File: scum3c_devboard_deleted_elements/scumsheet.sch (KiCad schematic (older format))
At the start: 16 parts, among them P5 Conn_01x02, U8 scum3

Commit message: added placeholder battery
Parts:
- removed P5: Conn_01x02, Connector_PinHeader_2.54mm:PinHeader_1x02_P2.54mm_Vertical, symbol Connector_Generic:Conn_01x02
- added BT1: Battery_Cell, symbol Device:Battery_Cell
- added P5: Conn_01x03, Connector_PinHeader_2.54mm:PinHeader_1x03_P2.54mm_Vertical, symbol Connector_Generic:Conn_01x03
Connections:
- wire segments 26 -> 23
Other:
- note added: "i know this isn't how it works. just getting a footprint placeholder\n"
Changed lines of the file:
@@
 GPIO0
-$Comp
-L Connector_Generic:Conn_01x02 P5
-U 1 1 5F3A4822
-P 9700 4850
-F 0 "P5" H 9618 5067 50  0000 C CNN
-F 1 "Conn_01x02" H 9618 4976 50  0000 C CNN
-F 2 "Connector_PinHeader_2.54mm:PinHeader_1x02_P2.54mm_Vertical" H 9700 4850 50  0001 C CNN
-F 3 "~" H 9700 4850 50  0001 C CNN
-	1    9700 4850
-	-1   0    0    -1
-$EndComp
 $Comp
 L draft1library:+VBAT #PWR0210
 U 1 1 5F3AF896
-P 10150 5050
+P 9800 5650
 AR Path="/5F3B1D81/5F3AF896" Ref="#PWR0210"  Part="1"
 AR Path="/5F41418C/5F3AF896" Ref="#PWR?"  Part="1"
 AR Path="/5F414989/5F3AF896" Ref="#PWR?"  Part="1"
-F 0 "#PWR0210" H 10150 4900 50  0001 C CNN
-F 1 "+VBAT" H 10165 5223 50  0000 C CNN
-F 2 "" H 10150 5050 50  0001 C CNN
-F 3 "" H 10150 5050 50  0001 C CNN
-	1    10150 5050
-	-1   0    0    1
+F 0 "#PWR0210" H 9800 5500 50  0001 C CNN
+F 1 "+VBAT" V 9800 5900 50  0000 C CNN
+F 2 "" H 9800 5650 50  0001 C CNN
+F 3 "" H 9800 5650 50  0001 C CNN
+	1    9800 5650
+	0    1    1    0
 $EndComp
-Wire Wire Line
-	10150 4950 10150 5050
-Wire Wire Line
-	9900 4950 10150 4950
-Wire Wire Line
-	9900 4850 10800 4850
-Text Label 10800 4850 2    50   ~ 0
+Text Label 9800 5450 0    50   ~ 0
 BOOT_SOURCE_SEL
 Wire Wire Line
@@
 	4750 6500 4750 6050
 $Comp
-L power:GND #PWR?
+L power:GND #PWR0109
 U 1 1 5F4F714B
 P 2250 4100
-AR Path="/5F3B1D81/5F4F714B" Ref="#PWR?"  Part="1"
+AR Path="/5F3B1D81/5F4F714B" Ref="#PWR0109"  Part="1"
 AR Path="/5F41418C/5F4F714B" Ref="#PWR?"  Part="1"
 AR Path="/5F414989/5F4F714B" Ref="#PWR?"  Part="1"
-F 0 "#PWR?" H 2250 3850 50  0001 C CNN
+F 0 "#PWR0109" H 2250 3850 50  0001 C CNN
 F 1 "GND" V 2255 3972 50  0000 R CNN
 F 2 "" H 2250 4100 50  0001 C CNN
@@
 NoConn ~ 6900 6050
 NoConn ~ 7050 6050
+$Comp
+L Connector_Generic:Conn_01x03 P5
+U 1 1 5F5126D4
+P 9600 5550
+F 0 "P5" H 9518 5225 50  0000 C CNN
+F 1 "Conn_01x03" H 9518 5316 50  0000 C CNN
+F 2 "Connector_PinHeader_2.54mm:PinHeader_1x03_P2.54mm_Vertical" H 9600 5550 50  0001 C CNN
+F 3 "~" H 9600 5550 50  0001 C CNN
+	1    9600 5550
+	-1   0    0    1
+$EndComp
+$Comp
+L draft1library:+VDDIO #PWR0110
+U 1 1 5F5148F6
+P 9800 5550
+F 0 "#PWR0110" H 9800 5400 50  0001 C CNN
+F 1 "+VDDIO" V 9815 5678 50  0000 L CNN
+F 2 "" H 9800 5550 50  0001 C CNN
+F 3 "" H 9800 5550 50  0001 C CNN
+	1    9800 5550
+	0    1    1    0
+$EndComp
+$Comp
+L Device:Battery_Cell BT1
+U 1 1 5F554877
+P 10300 4300
+F 0 "BT1" H 10418 4396 50  0000 L CNN
+F 1 "Battery_Cell" H 10418 4305 50  0000 L CNN
+F 2 "" V 10300 4360 50  0001 C CNN
+F 3 "~" V 10300 4360 50  0001 C CNN
+	1    10300 4300
+	1    0    0    -1
+$EndComp
+$Comp
+L power:GND #PWR0120
+U 1 1 5F555029
+P 10300 4400
+F 0 "#PWR0120" H 10300 4150 50  0001 C CNN
+F 1 "GND" H 10305 4227 50  0000 C CNN
+F 2 "" H 10300 4400 50  0001 C CNN
+F 3 "" H 10300 4400 50  0001 C CNN
+	1    10300 4400
+	1    0    0    -1
+$EndComp
+$Comp
+L draft1library:+VBAT #PWR0121
+U 1 1 5F5558C9
+P 10300 4100
+F 0 "#PWR0121" H 10300 3950 50  0001 C CNN
+F 1 "+VBAT" H 10315 4273 50  0000 C CNN
+F 2 "" H 10300 4100 50  0001 C CNN
+F 3 "" H 10300 4100 50  0001 C CNN
+	1    10300 4100
+	1    0    0    -1
+$EndComp
+Text Notes 8600 4850 0    50   ~ 0
+i know this isn't how it works. just getting a footprint placeholder\n
 $EndSCHEMATC

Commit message: battery footprint
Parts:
- BT1: footprint (none) -> Battery:Battery_Panasonic_CR2032-VS1N_Vertical_CircularHoles
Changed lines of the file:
@@
-$EndComp
-$Comp
-L Device:Battery_Cell BT1
-U 1 1 5F554877
-P 10300 4300
-F 0 "BT1" H 10418 4396 50  0000 L CNN
-F 1 "Battery_Cell" H 10418 4305 50  0000 L CNN
-F 2 "" V 10300 4360 50  0001 C CNN
-F 3 "~" V 10300 4360 50  0001 C CNN
-	1    10300 4300
-	1    0    0    -1
 $EndComp
 $Comp
@@
 Text Notes 8600 4850 0    50   ~ 0
 i know this isn't how it works. just getting a footprint placeholder\n
+$Comp
+L Device:Battery_Cell BT1
+U 1 1 5F554877
+P 10300 4300
+F 0 "BT1" H 10418 4396 50  0000 L CNN
+F 1 "Battery_Cell" H 10418 4305 50  0000 L CNN
+F 2 "Battery:Battery_Panasonic_CR2032-VS1N_Vertical_CircularHoles" V 10300 4360 50  0001 C CNN
+F 3 "~" V 10300 4360 50  0001 C CNN
+	1    10300 4300
+	1    0    0    -1
+$EndComp
 $EndSCHEMATC

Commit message: added zener diode voltage protection
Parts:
- U8: footprint SCUM:QFN-100_EP_12x12_Pitch0.4mm -> SCUM:QFN-100_EP_12x12_Pitch0.4mm_Margin0.25mm
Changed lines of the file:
@@
 Wire Wire Line
 	4750 6500 4750 6050
-$Comp
-L power:GND #PWR0109
-U 1 1 5F4F714B
-P 2250 4100
-AR Path="/5F3B1D81/5F4F714B" Ref="#PWR0109"  Part="1"
-AR Path="/5F41418C/5F4F714B" Ref="#PWR?"  Part="1"
-AR Path="/5F414989/5F4F714B" Ref="#PWR?"  Part="1"
-F 0 "#PWR0109" H 2250 3850 50  0001 C CNN
-F 1 "GND" V 2255 3972 50  0000 R CNN
-F 2 "" H 2250 4100 50  0001 C CNN
-F 3 "" H 2250 4100 50  0001 C CNN
-	1    2250 4100
-	0    1    1    0
-$EndComp
 NoConn ~ 8000 3000
 NoConn ~ 8000 3150
@@
 F 0 "U8" H 8944 3271 50  0000 L CNN
 F 1 "scum3" H 8944 3180 50  0000 L CNN
-F 2 "SCUM:QFN-100_EP_12x12_Pitch0.4mm" H 5200 3450 50  0001 C CNN
+F 2 "SCUM:QFN-100_EP_12x12_Pitch0.4mm_Margin0.25mm" H 5200 3450 50  0001 C CNN
 F 3 "" H 5200 3450 50  0001 C CNN
 	1    5200 3450
@@
 	1    0    0    -1
 $EndComp
+$Comp
+L power:GND #PWR0109
+U 1 1 5F4F714B
+P 2250 4100
+AR Path="/5F3B1D81/5F4F714B" Ref="#PWR0109"  Part="1"
+AR Path="/5F41418C/5F4F714B" Ref="#PWR?"  Part="1"
+AR Path="/5F414989/5F4F714B" Ref="#PWR?"  Part="1"
+F 0 "#PWR0109" H 2250 3850 50  0001 C CNN
+F 1 "GND" V 2255 3972 50  0000 R CNN
+F 2 "" H 2250 4100 50  0001 C CNN
+F 3 "" H 2250 4100 50  0001 C CNN
+	1    2250 4100
+	0    1    1    0
+$EndComp
 $EndSCHEMATC

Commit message: added LED
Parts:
- removed BT1: Battery_Cell, Battery:Battery_Panasonic_CR2032-VS1N_Vertical_CircularHoles, symbol Device:Battery_Cell
- removed P5: Conn_01x03, Connector_PinHeader_2.54mm:PinHeader_1x03_P2.54mm_Vertical, symbol Connector_Generic:Conn_01x03
- added LED1: LD_MVSG-JGLH-46-1, LEDM2218X140N, symbol SamacSys_Parts:LD_MVSG-JGLH-46-1
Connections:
- net labels added: 3WB_CLK, 3WB_DATA, 3WB_ENB, RF_IN, RsRx, RsTx
- wire segments 23 -> 24
- no-connect marks 58 -> 52
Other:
- note removed: "i know this isn't how it works. just getting a footprint placeholder\n"
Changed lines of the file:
@@
 NoConn ~ 8000 2100
 NoConn ~ 8000 2250
-NoConn ~ 8000 4650
 NoConn ~ 8000 5550
 NoConn ~ 8000 5400
@@
 Wire Wire Line
 	8000 4050 9250 4050
-Text Label 9250 4050 2    50   ~ 0
-BOOT_SOURCE_SEL
 $Comp
 L Device:C C20
@@
 Text HLabel 3700 6050 3    50   BiDi ~ 0
 GPIO0
-$Comp
-L draft1library:+VBAT #PWR0210
-U 1 1 5F3AF896
-P 9800 5650
-AR Path="/5F3B1D81/5F3AF896" Ref="#PWR0210"  Part="1"
-AR Path="/5F41418C/5F3AF896" Ref="#PWR?"  Part="1"
-AR Path="/5F414989/5F3AF896" Ref="#PWR?"  Part="1"
-F 0 "#PWR0210" H 9800 5500 50  0001 C CNN
-F 1 "+VBAT" V 9800 5900 50  0000 C CNN
-F 2 "" H 9800 5650 50  0001 C CNN
-F 3 "" H 9800 5650 50  0001 C CNN
-	1    9800 5650
-	0    1    1    0
-$EndComp
-Text Label 9800 5450 0    50   ~ 0
-BOOT_SOURCE_SEL
 Wire Wire Line
 	4300 6050 4300 6500
@@
 	1    0    0    -1
 $EndComp
-NoConn ~ 6450 6050
-NoConn ~ 6600 6050
-NoConn ~ 6750 6050
-NoConn ~ 6900 6050
-NoConn ~ 7050 6050
-$Comp
-L Connector_Generic:Conn_01x03 P5
-U 1 1 5F5126D4
-P 9600 5550
-F 0 "P5" H 9518 5225 50  0000 C CNN
-F 1 "Conn_01x03" H 9518 5316 50  0000 C CNN
-F 2 "Connector_PinHeader_2.54mm:PinHeader_1x03_P2.54mm_Vertical" H 9600 5550 50  0001 C CNN
-F 3 "~" H 9600 5550 50  0001 C CNN
-	1    9600 5550
+Text HLabel 6750 6050 3    50   BiDi ~ 0
+3WB_CLK
+Text HLabel 6900 6050 3    50   BiDi ~ 0
+3WB_ENB
+Text HLabel 7050 6050 3    50   BiDi ~ 0
+3WB_DATA
+Text HLabel 2250 4100 0    50   BiDi ~ 0
+RF_IN
+Text HLabel 6450 6050 3    50   BiDi ~ 0
+RsTx
+Text HLabel 6600 6050 3    50   BiDi ~ 0
+RsRx
+Text HLabel 9250 4050 2    50   BiDi ~ 0
+BOOT_SOURCE_SEL
+$Comp
+L SamacSys_Parts:LD_MVSG-JGLH-46-1 LED1
+U 1 1 5F7B4972
+P 9200 4650
+F 0 "LED1" H 9500 4385 50  0000 C CNN
+F 1 "LD_MVSG-JGLH-46-1" H 9500 4476 50  0000 C CNN
+F 2 "LEDM2218X140N" H 9700 4800 50  0001 L BNN
+F 3 "https://dammedia.osram.info/media/resource/hires/osram-dam-6917470/LD%20MVSG_EN.pdf" H 9700 4700 50  0001 L BNN
+F 4 "Osram Opto LD MVSG-JGLH-46-1, Mini TOPLED Series Blue LED, 465 nm,, Rectangle Lens SMD Package" H 9700 4600 50  0001 L BNN "Description"
+F 5 "1.4" H 9700 4500 50  0001 L BNN "Height"
+F 6 "OSRAM" H 9700 4400 50  0001 L BNN "Manufacturer_Name"
+F 7 "LD MVSG-JGLH-46-1" H 9700 4300 50  0001 L BNN "Manufacturer_Part_Number"
+F 8 "LD MVSG-JGLH-46-1" H 9700 4200 50  0001 L BNN "Arrow Part Number"
+F 9 "https://www.arrow.com/en/products/ldmvsg-jglh-46-1/osram-opto-semiconductors" H 9700 4100 50  0001 L BNN "Arrow Price/Stock"
+F 10 "720-LDMVSGJGLH461" H 9700 4000 50  0001 L BNN "Mouser Part Number"
+F 11 "https://www.mouser.co.uk/ProductDetail/OSRAM-Opto-Semiconductors/LD-MVSG-JGLH-46-1?qs=znB0%2F8lYn%252BuYpqaPHtqGHw%3D%3D" H 9700 3900 50  0001 L BNN "Mouser Price/Stock"
+	1    9200 4650
 	-1   0    0    1
 $EndComp
-$Comp
-L draft1library:+VDDIO #PWR0110
-U 1 1 5F5148F6
-P 9800 5550
-F 0 "#PWR0110" H 9800 5400 50  0001 C CNN
-F 1 "+VDDIO" V 9815 5678 50  0000 L CNN
-F 2 "" H 9800 5550 50  0001 C CNN
-F 3 "" H 9800 5550 50  0001 C CNN
-	1    9800 5550
-	0    1    1    0
-$EndComp
-$Comp
-L power:GND #PWR0120
-U 1 1 5F555029
-P 10300 4400
-F 0 "#PWR0120" H 10300 4150 50  0001 C CNN
-F 1 "GND" H 10305 4227 50  0000 C CNN
-F 2 "" H 10300 4400 50  0001 C CNN
-F 3 "" H 10300 4400 50  0001 C CNN
-	1    10300 4400
-	1    0    0    -1
-$EndComp
-$Comp
-L draft1library:+VBAT #PWR0121
-U 1 1 5F5558C9
-P 10300 4100
-F 0 "#PWR0121" H 10300 3950 50  0001 C CNN
-F 1 "+VBAT" H 10315 4273 50  0000 C CNN
-F 2 "" H 10300 4100 50  0001 C CNN
-F 3 "" H 10300 4100 50  0001 C CNN
-	1    10300 4100
-	1    0    0    -1
-$EndComp
-Text Notes 8600 4850 0    50   ~ 0
-i know this isn't how it works. just getting a footprint placeholder\n
-$Comp
-L Device:Battery_Cell BT1
-U 1 1 5F554877
-P 10300 4300
-F 0 "BT1" H 10418 4396 50  0000 L CNN
-F 1 "Battery_Cell" H 10418 4305 50  0000 L CNN
-F 2 "Battery:Battery_Panasonic_CR2032-VS1N_Vertical_CircularHoles" V 10300 4360 50  0001 C CNN
-F 3 "~" V 10300 4360 50  0001 C CNN
-	1    10300 4300
-	1    0    0    -1
-$EndComp
-$Comp
-L power:GND #PWR0109
-U 1 1 5F4F714B
-P 2250 4100
-AR Path="/5F3B1D81/5F4F714B" Ref="#PWR0109"  Part="1"
-AR Path="/5F41418C/5F4F714B" Ref="#PWR?"  Part="1"
-AR Path="/5F414989/5F4F714B" Ref="#PWR?"  Part="1"
-F 0 "#PWR0109" H 2250 3850 50  0001 C CNN
-F 1 "GND" V 2255 3972 50  0000 R CNN
-F 2 "" H 2250 4100 50  0001 C CNN
-F 3 "" H 2250 4100 50  0001 C CNN
-	1    2250 4100
-	0    1    1    0
+Wire Wire Line
+	8000 4650 8600 4650
+$Comp
+L power:GND #PWR?
+U 1 1 5F7B7D3D
+P 9200 4650
+F 0 "#PWR?" H 9200 4400 50  0001 C CNN
+F 1 "GND" V 9205 4522 50  0000 R CNN
+F 2 "" H 9200 4650 50  0001 C CNN
+F 3 "" H 9200 4650 50  0001 C CNN
+	1    9200 4650
+	0    -1   -1   0
 $EndComp
 $EndSCHEMATC

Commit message: moved pins
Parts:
- LED1: footprint LEDM2218X140N -> SamacSys_Parts:LEDM2218X140N
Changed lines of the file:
@@
 F 0 "LED1" H 9500 4385 50  0000 C CNN
 F 1 "LD_MVSG-JGLH-46-1" H 9500 4476 50  0000 C CNN
-F 2 "LEDM2218X140N" H 9700 4800 50  0001 L BNN
+F 2 "SamacSys_Parts:LEDM2218X140N" H 9700 4800 50  0001 L BNN
 F 3 "https://dammedia.osram.info/media/resource/hires/osram-dam-6917470/LD%20MVSG_EN.pdf" H 9700 4700 50  0001 L BNN
 F 4 "Osram Opto LD MVSG-JGLH-46-1, Mini TOPLED Series Blue LED, 465 nm,, Rectangle Lens SMD Package" H 9700 4600 50  0001 L BNN "Description"
@@
 	8000 4650 8600 4650
 $Comp
-L power:GND #PWR?
+L power:GND #PWR0125
 U 1 1 5F7B7D3D
 P 9200 4650
-F 0 "#PWR?" H 9200 4400 50  0001 C CNN
+F 0 "#PWR0125" H 9200 4400 50  0001 C CNN
 F 1 "GND" V 9205 4522 50  0000 R CNN
 F 2 "" H 9200 4650 50  0001 C CNN

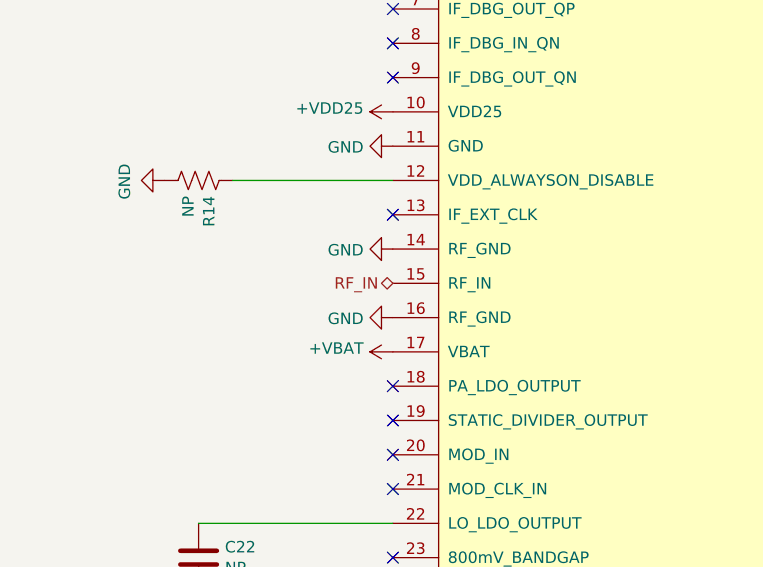
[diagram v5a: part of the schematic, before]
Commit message: replaced headers with smaller ones
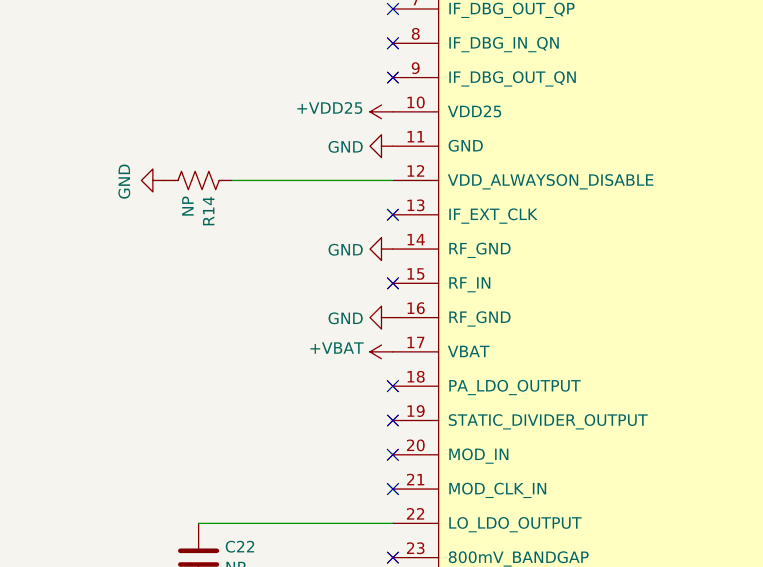
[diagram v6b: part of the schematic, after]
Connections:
- net RF_IN: no longer names the net of U8.15 (RF_IN)
- no-connect marks 52 -> 53
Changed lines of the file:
@@
 Wire Wire Line
 	8000 2550 9150 2550
-$Comp
-L draft1library:scum3 U8
-U 1 1 5F3B2246
-P 5200 3450
-AR Path="/5F3B1D81/5F3B2246" Ref="U8"  Part="1"
-AR Path="/5F41418C/5F3B2246" Ref="U?"  Part="1"
-AR Path="/5F414989/5F3B2246" Ref="U?"  Part="1"
-F 0 "U8" H 8944 3271 50  0000 L CNN
-F 1 "scum3" H 8944 3180 50  0000 L CNN
-F 2 "SCUM:QFN-100_EP_12x12_Pitch0.4mm_Margin0.25mm" H 5200 3450 50  0001 C CNN
-F 3 "" H 5200 3450 50  0001 C CNN
-	1    5200 3450
-	1    0    0    -1
-$EndComp
 Text HLabel 6750 6050 3    50   BiDi ~ 0
 3WB_CLK
@@
 Text HLabel 7050 6050 3    50   BiDi ~ 0
 3WB_DATA
-Text HLabel 2250 4100 0    50   BiDi ~ 0
-RF_IN
 Text HLabel 6450 6050 3    50   BiDi ~ 0
 RsTx
@@
 	0    -1   -1   0
 $EndComp
+$Comp
+L draft1library:scum3 U8
+U 1 1 5F3B2246
+P 5200 3450
+AR Path="/5F3B1D81/5F3B2246" Ref="U8"  Part="1"
+AR Path="/5F41418C/5F3B2246" Ref="U?"  Part="1"
+AR Path="/5F414989/5F3B2246" Ref="U?"  Part="1"
+F 0 "U8" H 8944 3271 50  0000 L CNN
+F 1 "scum3" H 8944 3180 50  0000 L CNN
+F 2 "SCUM:QFN-100_EP_12x12_Pitch0.4mm_Margin0.25mm" H 5200 3450 50  0001 C CNN
+F 3 "" H 5200 3450 50  0001 C CNN
+	1    5200 3450
+	1    0    0    -1
+$EndComp
+NoConn ~ 2250 4100
 $EndSCHEMATC

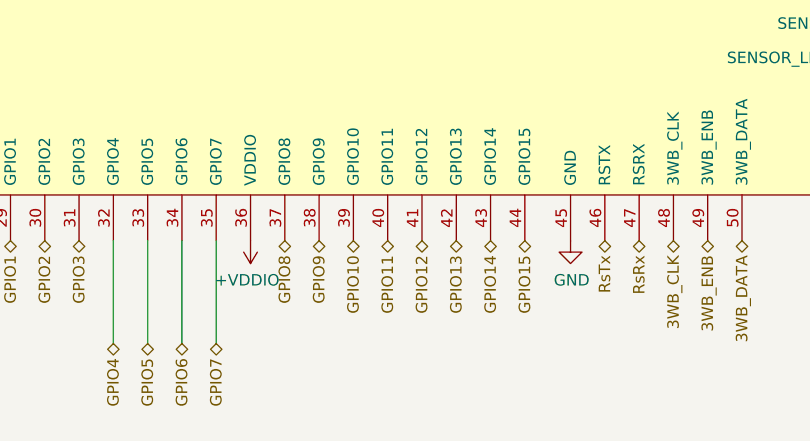
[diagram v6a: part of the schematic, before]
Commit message: routed traces
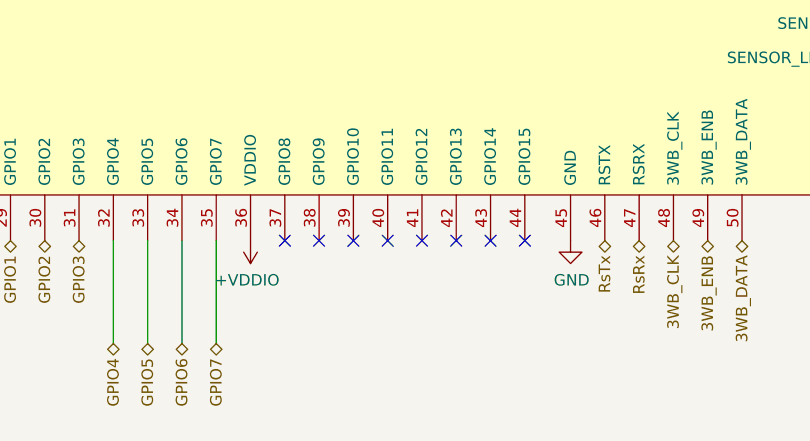
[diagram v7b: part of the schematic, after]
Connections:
- net GPIO10: no longer names the net of U8.39 (GPIO10)
- net GPIO11: no longer names the net of U8.40 (GPIO11)
- net GPIO12: no longer names the net of U8.41 (GPIO12)
- net GPIO13: no longer names the net of U8.42 (GPIO13)
- net GPIO14: no longer names the net of U8.43 (GPIO14)
- net GPIO15: no longer names the net of U8.44 (GPIO15)
- net GPIO8: no longer names the net of U8.37 (GPIO8)
- net GPIO9: no longer names the net of U8.38 (GPIO9)
- no-connect marks 53 -> 61
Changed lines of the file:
@@
 Text HLabel 4750 6500 3    50   BiDi ~ 0
 GPIO7
-Text HLabel 5050 6050 3    50   BiDi ~ 0
-GPIO8
-Text HLabel 5200 6050 3    50   BiDi ~ 0
-GPIO9
-Text HLabel 5350 6050 3    50   BiDi ~ 0
-GPIO10
-Text HLabel 5500 6050 3    50   BiDi ~ 0
-GPIO11
-Text HLabel 5650 6050 3    50   BiDi ~ 0
-GPIO12
-Text HLabel 5800 6050 3    50   BiDi ~ 0
-GPIO13
-Text HLabel 5950 6050 3    50   BiDi ~ 0
-GPIO14
-Text HLabel 6100 6050 3    50   BiDi ~ 0
-GPIO15
 $Comp
 L draft1library:+VDDIO #PWR0194
@@
 $EndComp
 NoConn ~ 2250 4100
+NoConn ~ 6100 6050
+NoConn ~ 5950 6050
+NoConn ~ 5800 6050
+NoConn ~ 5650 6050
+NoConn ~ 5500 6050
+NoConn ~ 5350 6050
+NoConn ~ 5200 6050
+NoConn ~ 5050 6050
 $EndSCHEMATC

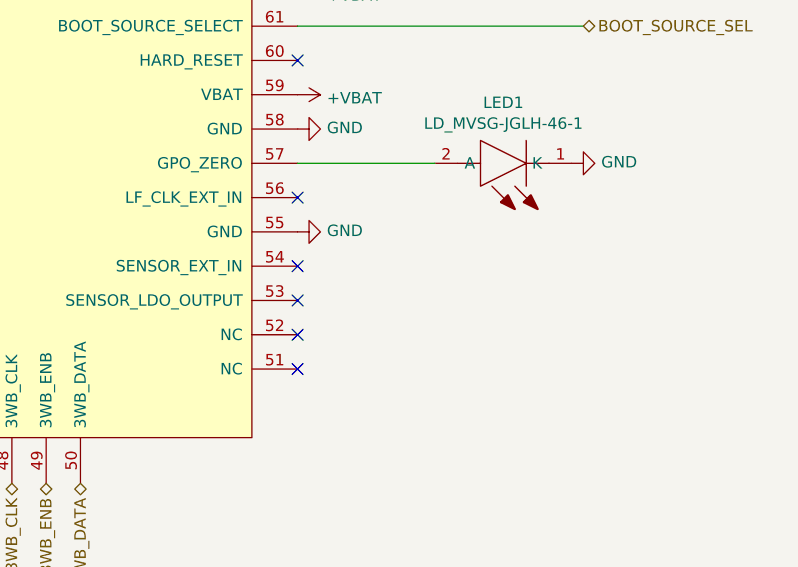
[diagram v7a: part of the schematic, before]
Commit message: added ADC pins
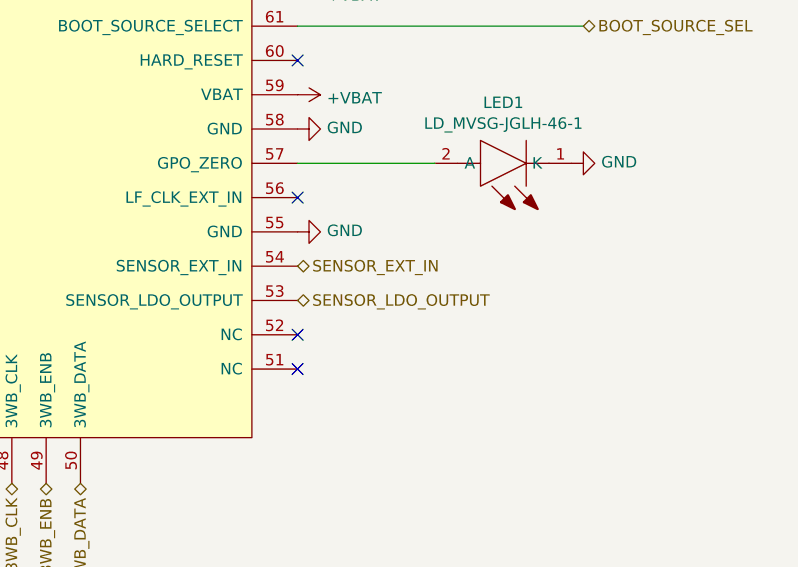
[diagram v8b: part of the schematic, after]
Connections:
- net SENSOR_LDO_OUTPUT: now reaches U8.53 (SENSOR_LDO_OUTPUT)
- net SENSOR_EXT_IN: now reaches U8.54 (SENSOR_EXT_IN)
- no-connect marks 61 -> 59
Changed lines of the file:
@@
 NoConn ~ 8000 5550
 NoConn ~ 8000 5400
-NoConn ~ 8000 5250
-NoConn ~ 8000 5100
 NoConn ~ 6950 1150
 NoConn ~ 6800 1150
@@
 NoConn ~ 5200 6050
 NoConn ~ 5050 6050
+Text HLabel 8000 5100 2    50   BiDi ~ 0
+SENSOR_EXT_IN
+Text HLabel 8000 5250 2    50   BiDi ~ 0
+SENSOR_LDO_OUTPUT
 $EndSCHEMATC
